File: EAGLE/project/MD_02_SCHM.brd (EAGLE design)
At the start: 52.1 x 59.2 mm, 48 parts, among them IC1 CA3140D, IC2 CA3140D, IC3 CD74HC4067M96E4, IC4 CD74HC4067M96E4, IC5 ADS1113IDGSR

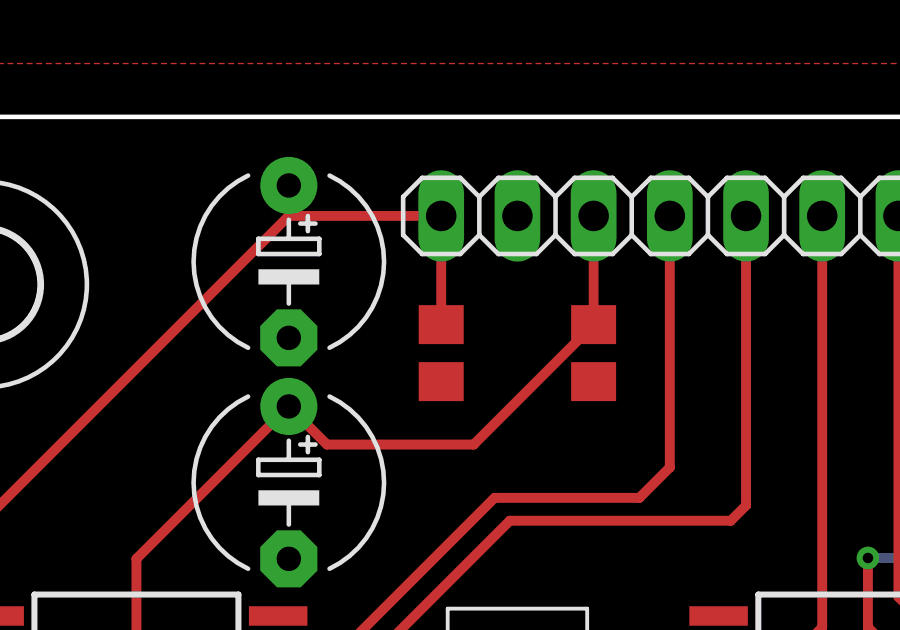
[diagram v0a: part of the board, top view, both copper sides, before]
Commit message: Updating EAGLE files and top/bottom layers PDF
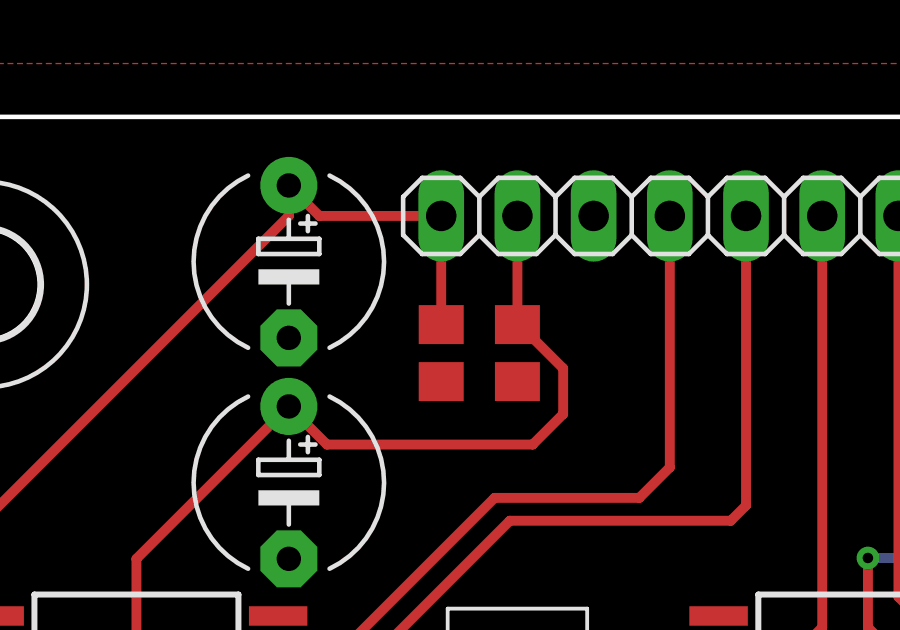
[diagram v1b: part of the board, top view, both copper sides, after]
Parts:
- moved C2 2.54 mm to (25.4, 51.3)
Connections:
- net 5V: now also JP3.2; no longer JP3.3
- net GND: now also JP3.3; no longer JP3.2
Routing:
- net 5V: track 145.4 -> 146.8 mm
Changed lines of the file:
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@@
 <attribute name="VALUE" x="21.59" y="52.705" size="1.27" layer="27"/>
 </element>
-<element name="C2" library="rcl" library_urn="urn:adsk.eagle:library:334" package="C0805" package3d_urn="urn:adsk.eagle:package:23617/2" value="100nF" x="27.94" y="51.308" smashed="yes" rot="R270">
-<attribute name="POPULARITY" value="63" x="45.72" y="51.308" size="1.778" layer="27" rot="R270" display="off"/>
-<attribute name="SPICEPREFIX" value="C" x="45.72" y="51.308" size="1.778" layer="27" rot="R270" display="off"/>
-<attribute name="VALUE" x="28.956" y="53.848" size="1.27" layer="27" rot="R270"/>
+<element name="C2" library="rcl" library_urn="urn:adsk.eagle:library:334" package="C0805" package3d_urn="urn:adsk.eagle:package:23617/2" value="100nF" x="25.4" y="51.308" smashed="yes" rot="R270">
+<attribute name="POPULARITY" value="63" x="43.18" y="51.308" size="1.778" layer="27" rot="R270" display="off"/>
+<attribute name="SPICEPREFIX" value="C" x="43.18" y="51.308" size="1.778" layer="27" rot="R270" display="off"/>
+<attribute name="VALUE" x="26.416" y="53.848" size="1.27" layer="27" rot="R270"/>
 </element>
 <element name="C3" library="rcl" library_urn="urn:adsk.eagle:library:334" package="C0805" package3d_urn="urn:adsk.eagle:package:23617/2" value="100nF" x="22.86" y="51.308" smashed="yes" rot="R90">
@@
 <attribute name="POPULARITY" value="4" x="5.08" y="54.356" size="1.778" layer="27" rot="R270" display="off"/>
 <attribute name="SPICEPREFIX" value="C" x="5.08" y="54.356" size="1.778" layer="27" rot="R270" display="off"/>
-<attribute name="VALUE" x="15.494" y="49.149" size="1.27" layer="27" ratio="10"/>
+<attribute name="VALUE" x="14.097" y="44.704" size="1.27" layer="27" ratio="10" rot="R90"/>
 </element>
 <element name="C5" library="rcl" library_urn="urn:adsk.eagle:library:334" package="E5-6" package3d_urn="urn:adsk.eagle:package:23368/1" value="220uF" x="17.78" y="46.99" smashed="yes" rot="R270">
@@
 <contactref element="C3" pad="1"/>
 <contactref element="C4" pad="-"/>
-<contactref element="JP3" pad="2"/>
+<contactref element="JP3" pad="3"/>
 </signal>
 <signal name="OUT">
@@
 <contactref element="C4" pad="+"/>
 <contactref element="JP3" pad="1"/>
-<wire x1="22.86" y1="52.258" x2="22.86" y2="55.88" width="0.3302" layer="1"/>
 <wire x1="17.78" y1="55.88" x2="17.78" y2="56.896" width="0.3302" layer="1"/>
 <wire x1="3.81" y1="41.91" x2="17.78" y2="55.88" width="0.3302" layer="1"/>
-<wire x1="22.86" y1="55.88" x2="17.78" y2="55.88" width="0.3302" layer="1"/>
+<wire x1="22.86" y1="55.88" x2="18.796" y2="55.88" width="0.3302" layer="1"/>
+<wire x1="18.796" y1="55.88" x2="17.78" y2="56.896" width="0.3302" layer="1"/>
+<wire x1="22.86" y1="52.258" x2="22.86" y2="55.88" width="0.3302" layer="1"/>
 </signal>
 <signal name="5V">
@@
 <contactref element="C2" pad="1"/>
 <contactref element="C5" pad="+"/>
-<contactref element="JP3" pad="3"/>
-<wire x1="27.94" y1="52.258" x2="27.94" y2="55.88" width="0.3302" layer="1"/>
-<wire x1="23.942" y1="48.26" x2="27.94" y2="52.258" width="0.3302" layer="1"/>
 <wire x1="12.7" y1="44.45" x2="17.78" y2="49.53" width="0.3302" layer="1"/>
 <wire x1="12.7" y1="30.48" x2="12.7" y2="44.45" width="0.3302" layer="1"/>
+<contactref element="JP3" pad="2"/>
+<wire x1="25.4" y1="52.258" x2="25.4" y2="55.88" width="0.3302" layer="1"/>
 <wire x1="17.78" y1="49.53" x2="19.05" y2="48.26" width="0.3302" layer="1"/>
-<wire x1="19.05" y1="48.26" x2="23.942" y2="48.26" width="0.3302" layer="1"/>
+<wire x1="25.908" y1="48.26" x2="26.924" y2="49.276" width="0.3302" layer="1"/>
+<wire x1="26.924" y1="49.276" x2="26.924" y2="50.8" width="0.3302" layer="1"/>
+<wire x1="26.924" y1="50.8" x2="25.466" y2="52.258" width="0.3302" layer="1"/>
+<wire x1="25.466" y1="52.258" x2="25.4" y2="52.258" width="0.3302" layer="1"/>
+<wire x1="19.05" y1="48.26" x2="25.908" y2="48.26" width="0.3302" layer="1"/>
 </signal>
 <signal name="DET3">

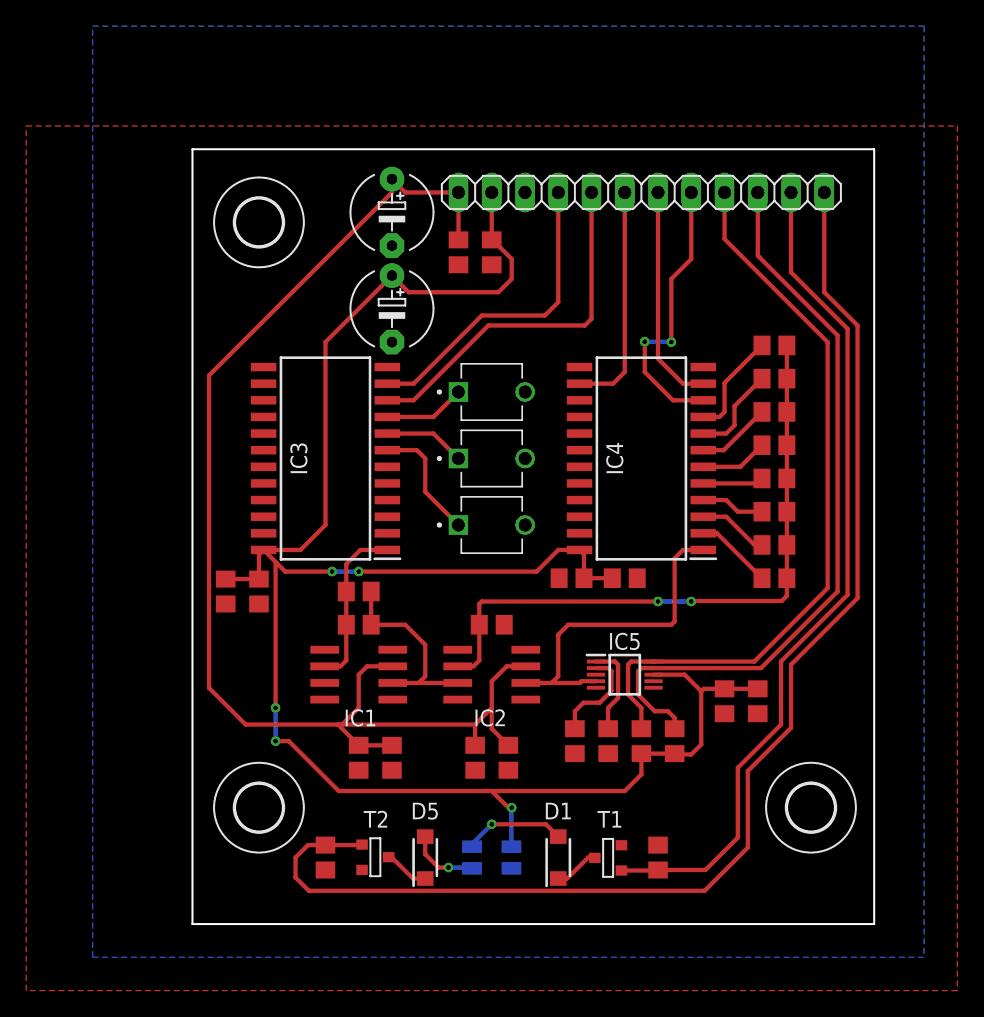
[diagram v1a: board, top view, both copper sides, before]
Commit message: Updated vias diameter and MUX footprint; Added GND vias; Polygon isolation changed to 24
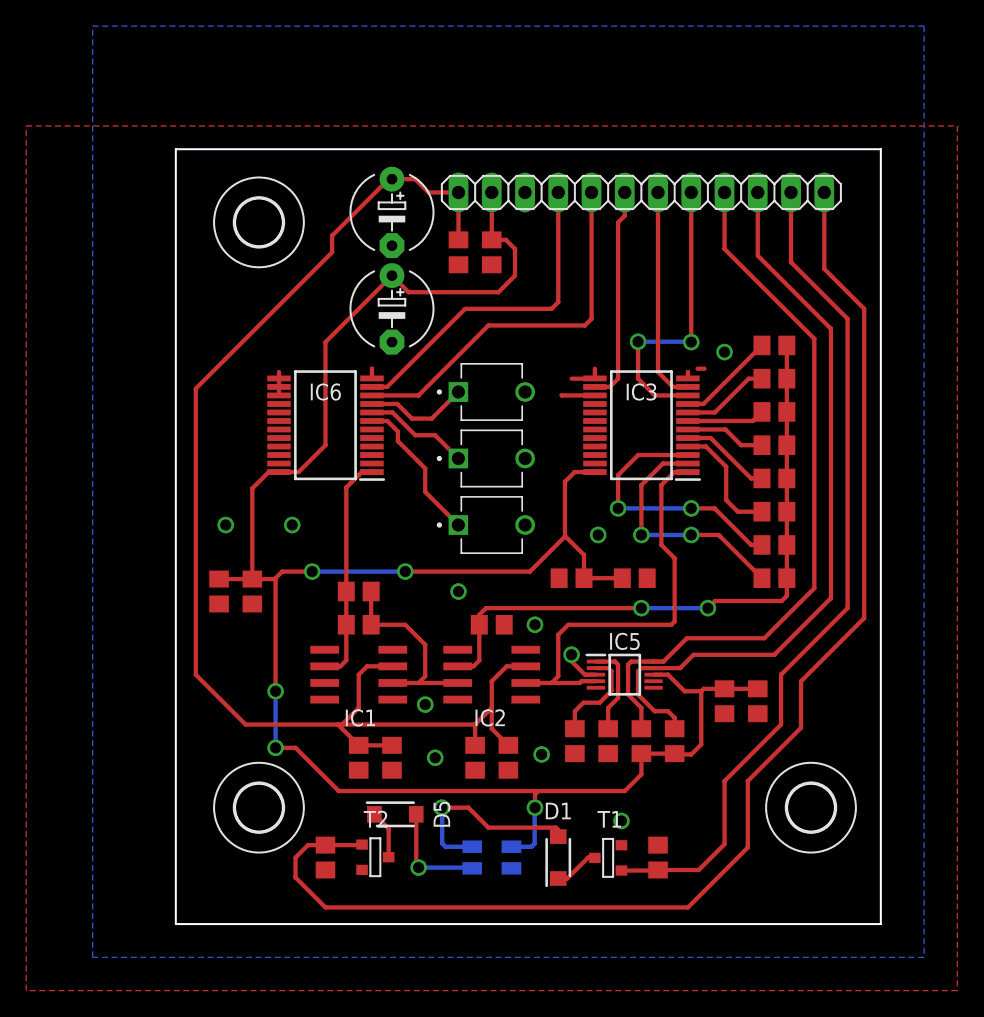
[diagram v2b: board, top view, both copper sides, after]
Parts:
- removed IC4: CD74HC4067M96E4, SamacSys_Parts:SOIC127P1030X265-24N
- added IC6: CD74HC4067SM96, CD74HC4067SM96:SOP65P780X200-24N
- IC3: value CD74HC4067M96E4 -> CD74HC4067SM96; device SamacSys_Parts:SOIC127P1030X265-24N -> CD74HC4067SM96:SOP65P780X200-24N
- moved IC3 24.3 mm to (36.8, 38.1)
- moved D5 4.02 mm to (18.0, 8.38), turned to 0 degrees
- moved C11 0.76 mm to (36.3, 26.4)
- moved C6 0.51 mm to (7.11, 25.4)
- moved C7 0.51 mm to (4.57, 25.4)
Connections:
- net 5V: now also IC6.24; no longer IC4.24
- net DET1: now also IC6.7; no longer IC3.7
- net DET2: now also IC6.8; no longer IC3.8
- net DET3: now also IC6.9; no longer IC3.9
- net G1: now also IC3.9; no longer IC4.9
- net G2: now also IC3.8; no longer IC4.8
- net G3: now also IC3.7; no longer IC4.7
- net G4: now also IC3.6; no longer IC4.6
- net G5: now also IC3.5; no longer IC4.5
- net G6: now also IC3.4; no longer IC4.4
- net G7: now also IC3.3; no longer IC4.3
- net G8: now also IC3.2; no longer IC4.2
- net GND: now also IC6.12, IC6.13, IC6.14, IC6.15; no longer IC3.14, IC4.12, IC4.13, IC4.15
- net OUT: now also IC3.1; no longer IC4.1
- net SD0: now also IC6.10; no longer IC3.10
- net SD1: now also IC6.11; no longer IC3.11
- net SG0: now also IC3.10; no longer IC4.10
- net SG1: now also IC3.11; no longer IC4.11
- net SG2: now also IC3.14; no longer IC4.14
- net TIA-: now also IC6.1; no longer IC3.1
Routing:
- net G7: track 5.38 -> 20.6 mm, vias 0 -> 2
- net G8: track 5.91 -> 18.6 mm, vias 0 -> 2
- net GND: track 0.00 -> 11.4 mm, vias 0 -> 11
- net 5V: track 146.8 -> 156.4 mm
- net N$3: track 7.80 -> 15.2 mm
- net OUT: track 25.9 -> 31.9 mm
- net TIA-: track 12.8 -> 17.5 mm
- net G6: track 4.85 -> 9.21 mm
- net N$4: track 5.38 -> 8.25 mm
- net G5: track 4.64 -> 7.48 mm
- net DET1: track 9.29 -> 11.4 mm
- net DET2: track 6.21 -> 8.06 mm
- net DET3: track 6.21 -> 7.90 mm
- net LED735: track 97.9 -> 99.4 mm
- net SCL: track 56.5 -> 55.0 mm
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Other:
- board size 52.1 x 59.2 mm -> 53.8 x 59.2 mm
